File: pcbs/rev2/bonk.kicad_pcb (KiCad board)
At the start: 2 copper layers, 246.5 x 83.9 mm, 151 parts, among them J1 Conn_01x04, J3 Conn_01x04, J4 USB_C_Receptacle_USB2.0_14P, Q1 2N7002, SW1 SW_Push, U1 XC6206PxxxMR, U2 STM32F072CBTx, U3 USBLC6-2SC6

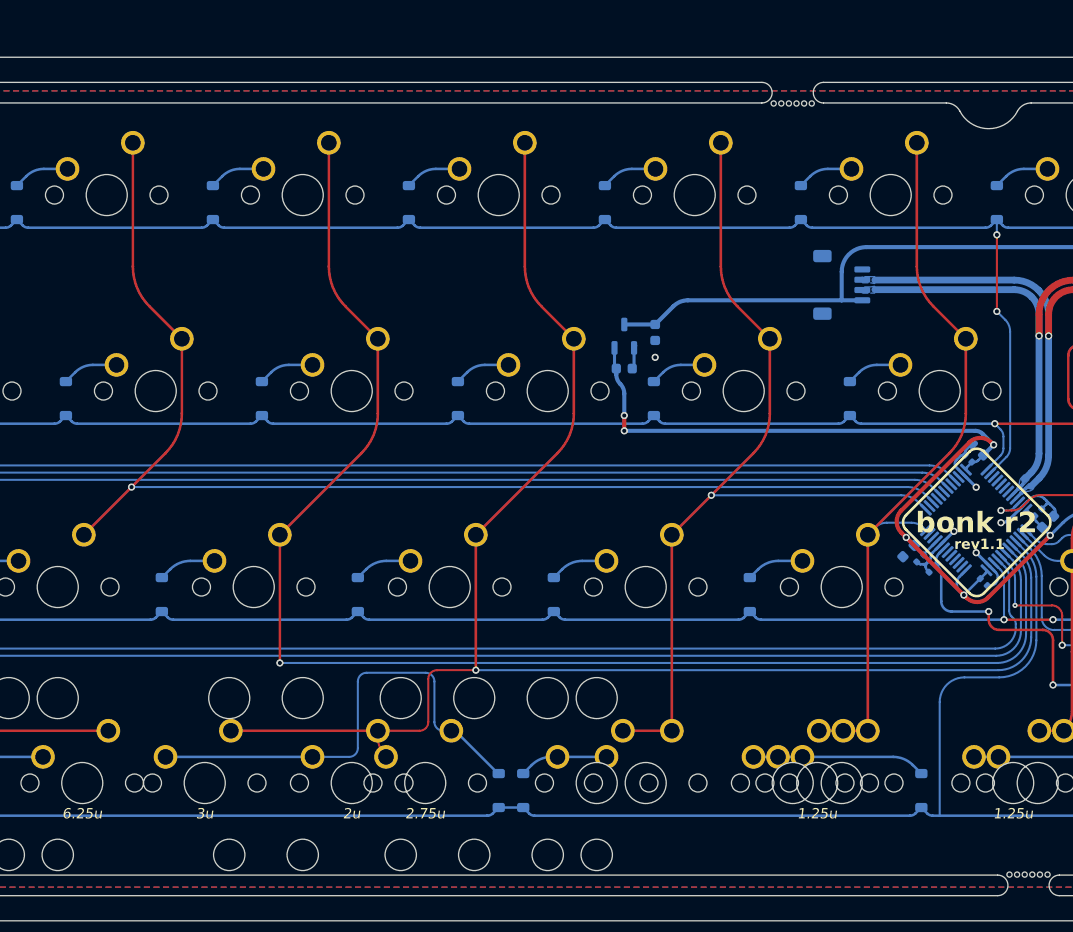
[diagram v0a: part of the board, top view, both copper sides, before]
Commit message: Added 2u stab mount points for 3u Spacebar option
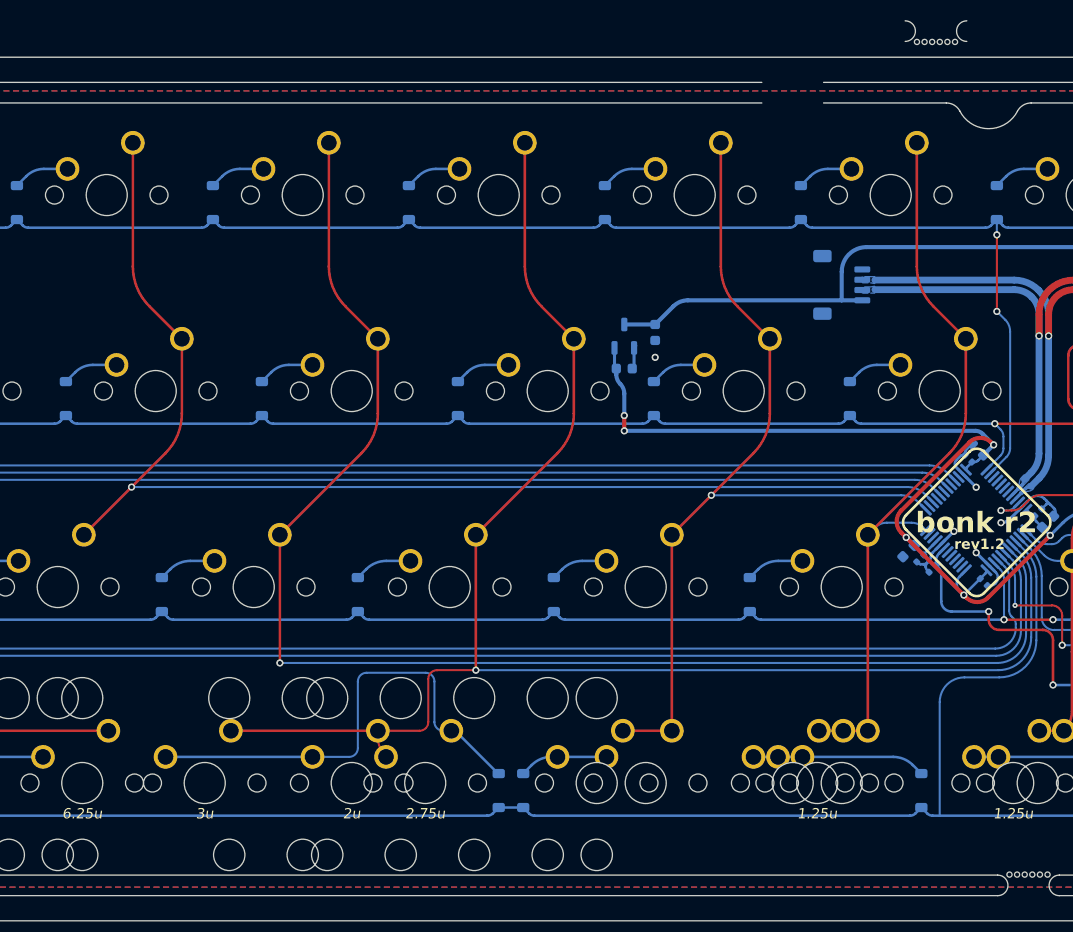
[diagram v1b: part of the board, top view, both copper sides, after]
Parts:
- added S9: 2, PCM_marbastlib-mx:STAB_MX_2u, F.Cu at (136.6, 79.5)
- moved REF** 15.2 mm to (207.7, 7.39)
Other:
- board text added: "rev1.2"
- board text removed: "rev1.1"
